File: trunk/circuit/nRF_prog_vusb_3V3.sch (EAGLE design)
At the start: 26 parts, among them Q2 12MHz

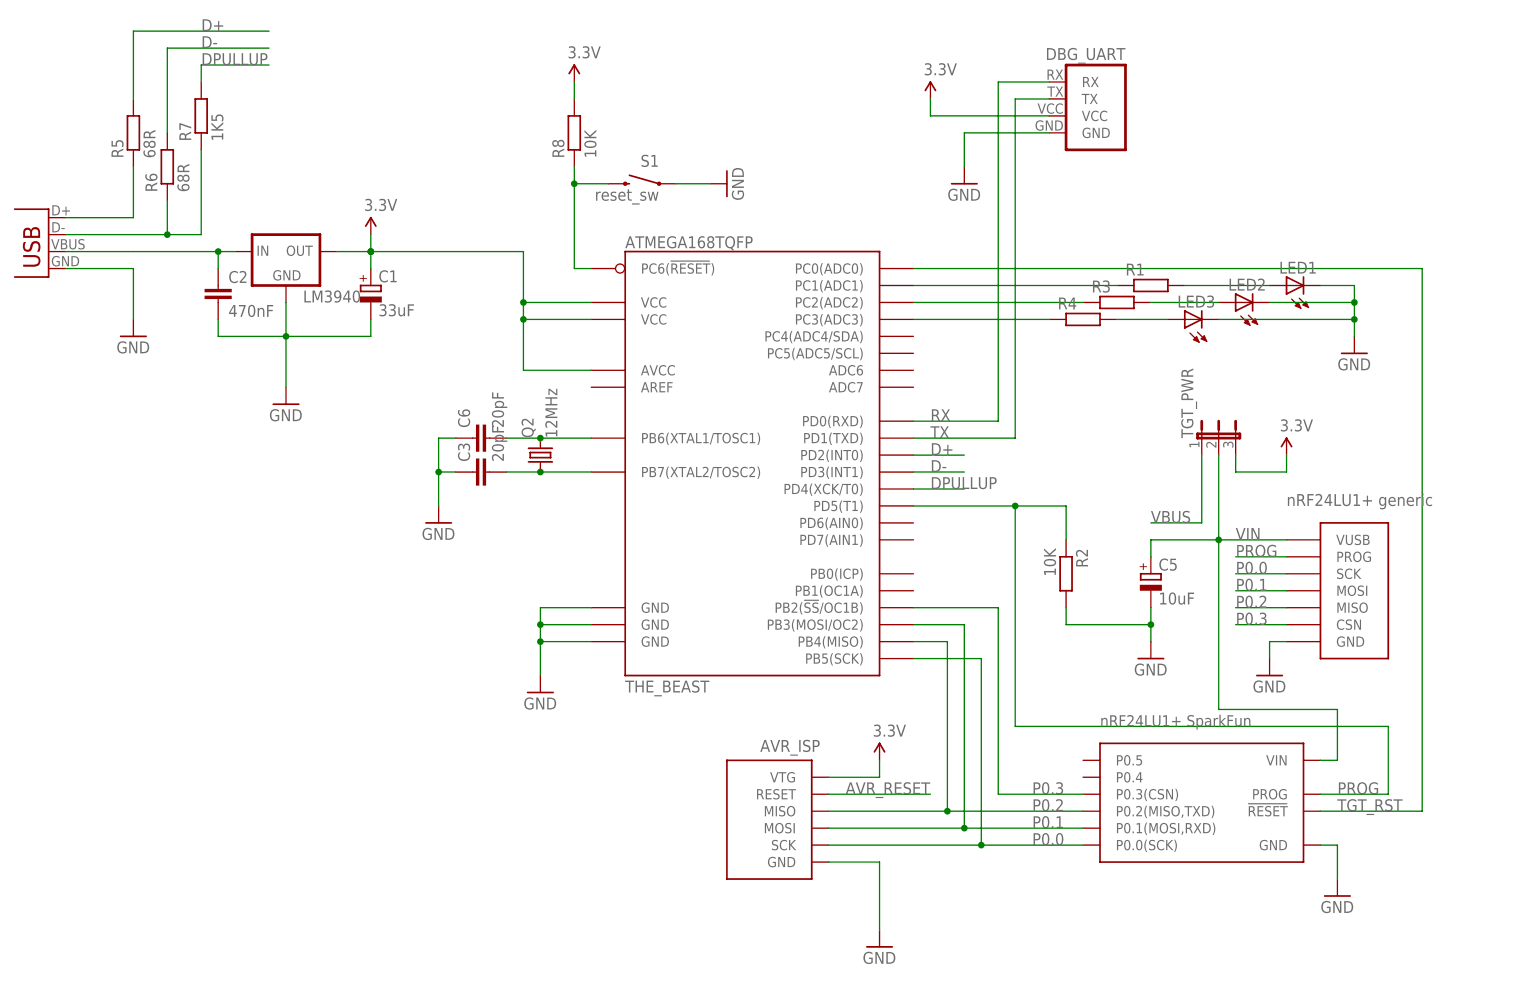
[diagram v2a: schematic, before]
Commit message: 
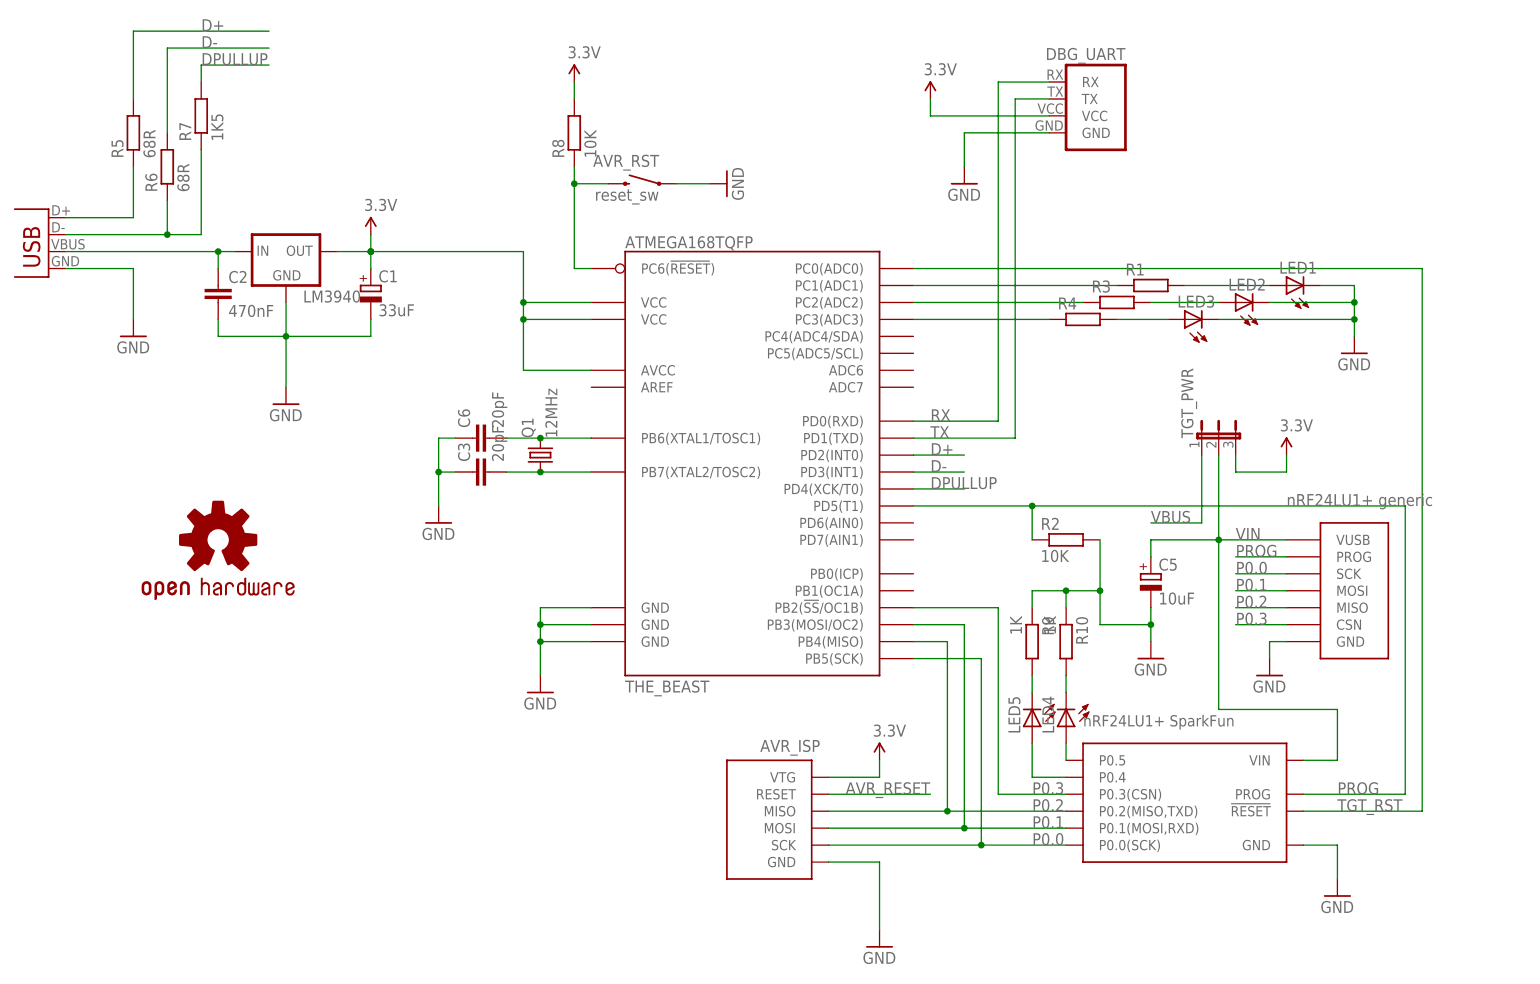
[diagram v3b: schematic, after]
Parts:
- removed U$2: NRF24LU1P_SPARKFUN_BREAKOUT, KileParts:NRF24LU1P_SPARKFUN_BREAKOUT
- added LED4, LED5: (no value), led:LEDCHIPLED_0805
- added LU1+_SPARKFUN: NRF24LU1P_SPARKFUN_BREAKOUT, KileParts:NRF24LU1P_SPARKFUN_BREAKOUT
- added R10, R9: 1K, rcl:R-EU_M0805
- added U$1: OSHW-LOGOM, SparkFun:OSHW-LOGOM
- TGT_PWR: device jumper:JP2E -> KileParts:JP2E
- renumbered NRF_GEN to LU1+_GENERIC, Q2 to Q1, S1 to AVR_RST
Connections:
- new net N$1: LED4.A, LU1+_SPARKFUN.P0.5
- new net N$2: LED5.A, LU1+_SPARKFUN.P0.4
- new net N$3: LED4.C, R10.2
- new net N$4: LED5.C, R9.2
- net GND: now also LU1+_SPARKFUN.GND, R10.1, R9.1; no longer U$2.GND
- net P0.0: now also LU1+_SPARKFUN.P0.0(SCK); no longer U$2.P0.0(SCK)
- net P0.1: now also LU1+_SPARKFUN.P0.1(MOSI,RXD); no longer U$2.P0.1(MOSI,RXD)
- net P0.2: now also LU1+_SPARKFUN.P0.2(MISO,TXD); no longer U$2.P0.2(MISO,TXD)
- net P0.3: now also LU1+_SPARKFUN.P0.3(CSN); no longer U$2.P0.3(CSN)
- net PROG: now also LU1+_SPARKFUN.PROG; no longer U$2.PROG
- net TGT_RST: now also LU1+_SPARKFUN.!RESET!; no longer U$2.!RESET!
- net VIN: now also LU1+_SPARKFUN.VIN; no longer U$2.VIN
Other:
- moved on the sheet: R2

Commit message: 
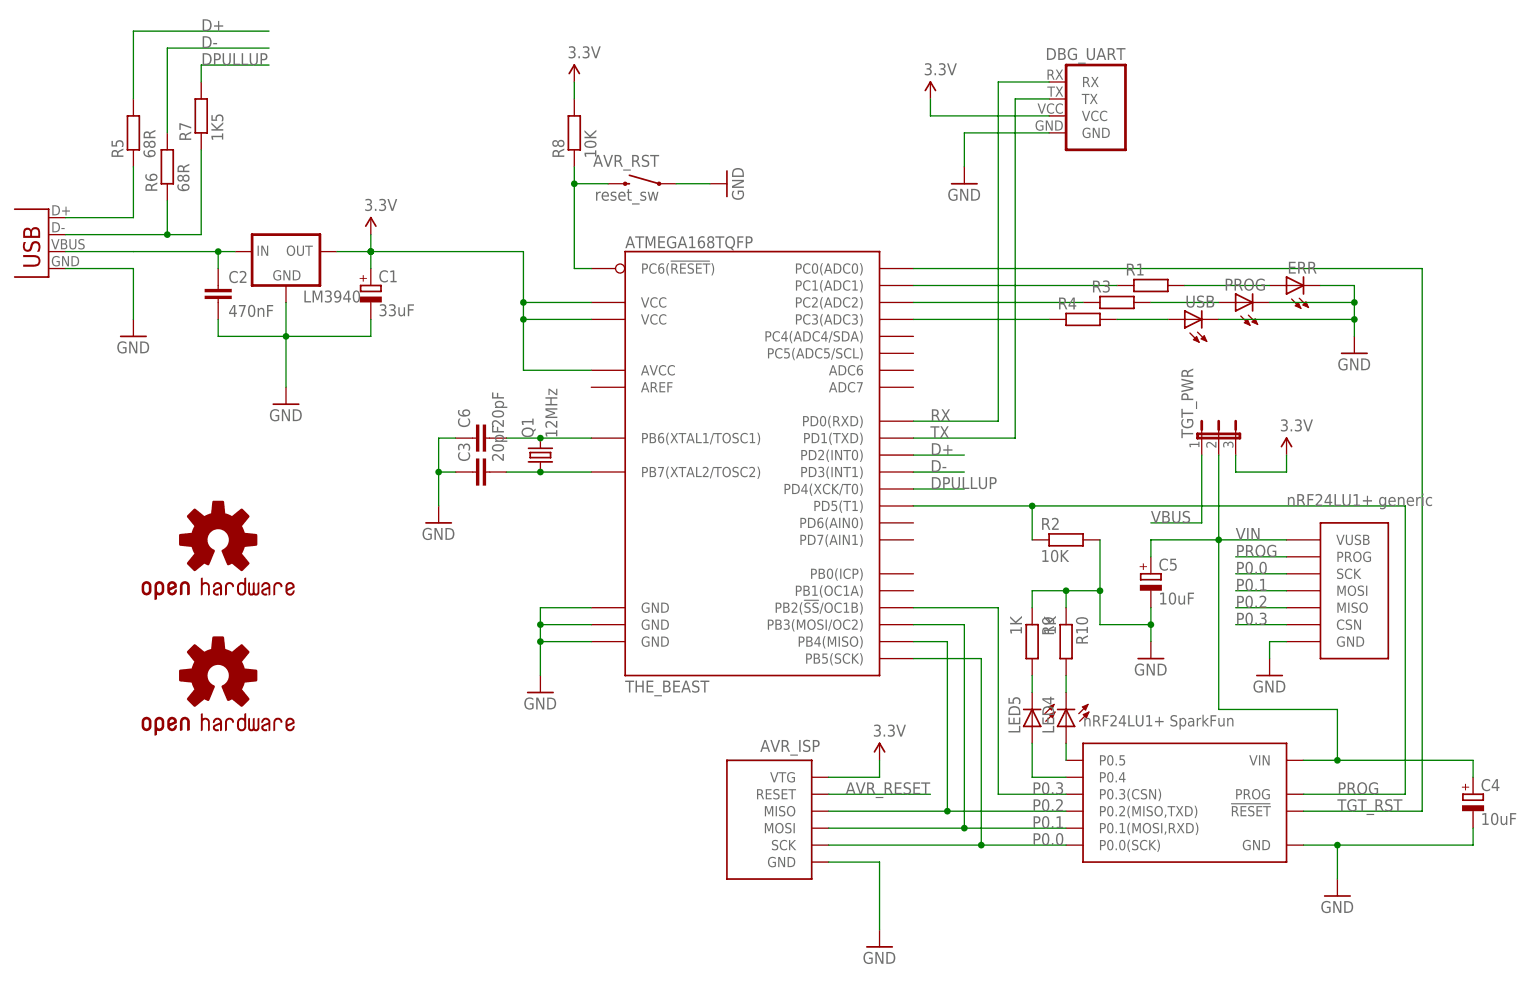
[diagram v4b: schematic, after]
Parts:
- added C4: 10uF, rcl:CPOL-EUSMCB
- added U$2: OSHW-LOGOL, SparkFun:OSHW-LOGOL
- renumbered LED1 to ERR, LED2 to PROG, LED3 to USB
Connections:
- net GND: now also C4.-
- net VIN: now also C4.+
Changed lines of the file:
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@@
 <part name="GND2" library="SparkFun" deviceset="GND" device=""/>
 <part name="C1" library="rcl" deviceset="CPOL-EU" device="SMCB" value="33uF"/>
-<part name="LED1" library="led" deviceset="LED" device="CHIPLED_0805"/>
+<part name="ERR" library="led" deviceset="LED" device="CHIPLED_0805"/>
 <part name="R1" library="rcl" deviceset="R-EU_" device="M0805"/>
 <part name="GND4" library="SparkFun" deviceset="GND" device=""/>
 <part name="C2" library="rcl" deviceset="C-EU" device="C0805K" value="470nF"/>
 <part name="R2" library="rcl" deviceset="R-EU_" device="M0805" value="10K"/>
-<part name="LED2" library="led" deviceset="LED" device="CHIPLED_0805"/>
+<part name="PROG" library="led" deviceset="LED" device="CHIPLED_0805"/>
 <part name="R3" library="rcl" deviceset="R-EU_" device="M0805"/>
-<part name="LED3" library="led" deviceset="LED" device="CHIPLED_0805"/>
+<part name="USB" library="led" deviceset="LED" device="CHIPLED_0805"/>
 <part name="R4" library="rcl" deviceset="R-EU_" device="M0805"/>
 <part name="THE_BEAST" library="KileParts" deviceset="ATMEGA168" device="TQFP" value="ATMEGA168TQFP"/>
@@
 <part name="R10" library="rcl" deviceset="R-EU_" device="M0805" value="1K"/>
 <part name="U$1" library="SparkFun" deviceset="OSHW-LOGO" device="M" value="OSHW-LOGOM"/>
+<part name="C4" library="rcl" deviceset="CPOL-EU" device="SMCB" value="10uF"/>
+<part name="U$2" library="SparkFun" deviceset="OSHW-LOGO" device="L" value="OSHW-LOGOL"/>
 </parts>
 <sheets>
@@
 <instance part="GND2" gate="1" x="-2.54" y="68.58"/>
 <instance part="C1" gate="G$1" x="10.16" y="86.36"/>
-<instance part="LED1" gate="G$1" x="147.32" y="86.36" rot="R90"/>
+<instance part="ERR" gate="G$1" x="147.32" y="86.36" rot="R90"/>
 <instance part="R1" gate="G$1" x="127" y="86.36"/>
 <instance part="GND4" gate="1" x="144.78" y="27.94"/>
 <instance part="C2" gate="G$1" x="-12.7" y="86.36"/>
 <instance part="R2" gate="G$1" x="114.3" y="48.26"/>
-<instance part="LED2" gate="G$1" x="139.7" y="83.82" rot="R90"/>
+<instance part="PROG" gate="G$1" x="139.7" y="83.82" rot="R90"/>
 <instance part="R3" gate="G$1" x="121.92" y="83.82"/>
-<instance part="LED3" gate="G$1" x="132.08" y="81.28" rot="R90"/>
+<instance part="USB" gate="G$1" x="132.08" y="81.28" rot="R90"/>
 <instance part="R4" gate="G$1" x="116.84" y="81.28"/>
 <instance part="THE_BEAST" gate="G$1" x="66.04" y="63.5"/>
@@
 <instance part="R10" gate="G$1" x="114.3" y="33.02" rot="R270"/>
 <instance part="U$1" gate="G$1" x="-12.7" y="48.26"/>
+<instance part="C4" gate="G$1" x="175.26" y="10.16"/>
+<instance part="U$2" gate="G$1" x="-12.7" y="27.94"/>
 </instances>
 <busses>
@@
 <wire x1="149.86" y1="2.54" x2="154.94" y2="2.54" width="0.1524" layer="91"/>
 <wire x1="154.94" y1="2.54" x2="154.94" y2="-2.54" width="0.1524" layer="91"/>
+<pinref part="C4" gate="G$1" pin="-"/>
+<wire x1="175.26" y1="5.08" x2="175.26" y2="2.54" width="0.1524" layer="91"/>
+<wire x1="175.26" y1="2.54" x2="154.94" y2="2.54" width="0.1524" layer="91"/>
+<junction x="154.94" y="2.54"/>
 </segment>
 <segment>
@@
 <segment>
 <wire x1="157.48" y1="83.82" x2="157.48" y2="86.36" width="0.1524" layer="91"/>
-<pinref part="LED2" gate="G$1" pin="C"/>
+<pinref part="PROG" gate="G$1" pin="C"/>
 <wire x1="144.78" y1="83.82" x2="157.48" y2="83.82" width="0.1524" layer="91"/>
-<pinref part="LED1" gate="G$1" pin="C"/>
+<pinref part="ERR" gate="G$1" pin="C"/>
 <wire x1="152.4" y1="86.36" x2="157.48" y2="86.36" width="0.1524" layer="91"/>
-<pinref part="LED3" gate="G$1" pin="C"/>
+<pinref part="USB" gate="G$1" pin="C"/>
 <wire x1="137.16" y1="81.28" x2="157.48" y2="81.28" width="0.1524" layer="91"/>
 <wire x1="157.48" y1="81.28" x2="157.48" y2="83.82" width="0.1524" layer="91"/>
@@
 <pinref part="TGT_PWR" gate="1" pin="2"/>
 <wire x1="137.16" y1="60.96" x2="137.16" y2="48.26" width="0.1524" layer="91"/>
+<pinref part="C4" gate="G$1" pin="+"/>
+<wire x1="154.94" y1="15.24" x2="175.26" y2="15.24" width="0.1524" layer="91"/>
+<wire x1="175.26" y1="15.24" x2="175.26" y2="12.7" width="0.1524" layer="91"/>
+<junction x="154.94" y="15.24"/>
 </segment>
 </net>
@@
 <segment>
 <pinref part="R4" gate="G$1" pin="2"/>
-<pinref part="LED3" gate="G$1" pin="A"/>
+<pinref part="USB" gate="G$1" pin="A"/>
 <wire x1="121.92" y1="81.28" x2="129.54" y2="81.28" width="0.1524" layer="91"/>
 </segment>
@@
 <segment>
 <pinref part="R3" gate="G$1" pin="2"/>
-<pinref part="LED2" gate="G$1" pin="A"/>
+<pinref part="PROG" gate="G$1" pin="A"/>
 <wire x1="127" y1="83.82" x2="137.16" y2="83.82" width="0.1524" layer="91"/>
 </segment>
@@
 <segment>
 <pinref part="R1" gate="G$1" pin="2"/>
-<pinref part="LED1" gate="G$1" pin="A"/>
+<pinref part="ERR" gate="G$1" pin="A"/>
 <wire x1="132.08" y1="86.36" x2="144.78" y2="86.36" width="0.1524" layer="91"/>
 </segment>
